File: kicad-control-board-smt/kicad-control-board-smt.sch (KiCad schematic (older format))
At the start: 97 parts, among them J101 Conn_01x10_Female, J102 Conn_01x16_Male, J103 BA56_3DIG_7SEG, J104 Gate Out, J105 Clock Out, J106 Clock In, J107 Pitch Out, J108 CV Out, J109 Reset In, Q101 MMBT3906, Q102 MMBT3906, Q103 MMBT3906, Q104 MMBT3904, Q105 MMBT3904, SW101 Shift, SW102 Play, SW103 Load, SW104 Save, SW105 Repeat, SW106 Mutate, SW107 Glide, SW108 SW_Push, SW109 SW_Push, SW110 SW_Push, SW111 SW_Push, SW112 SW_Push, SW113 SW_Push, SW114 SW_Push, SW115 SW_Push, SW116 Rotary_Encoder, SW117 SW_Push, SW118 SW_Push, SW119 SW_Push, SW120 SW_Push, SW121 SW_Push, SW122 SW_Push, SW123 SW_Push, SW124 SW_Push, U101 74HC595, U102 MCP23S17, U103 74HC595

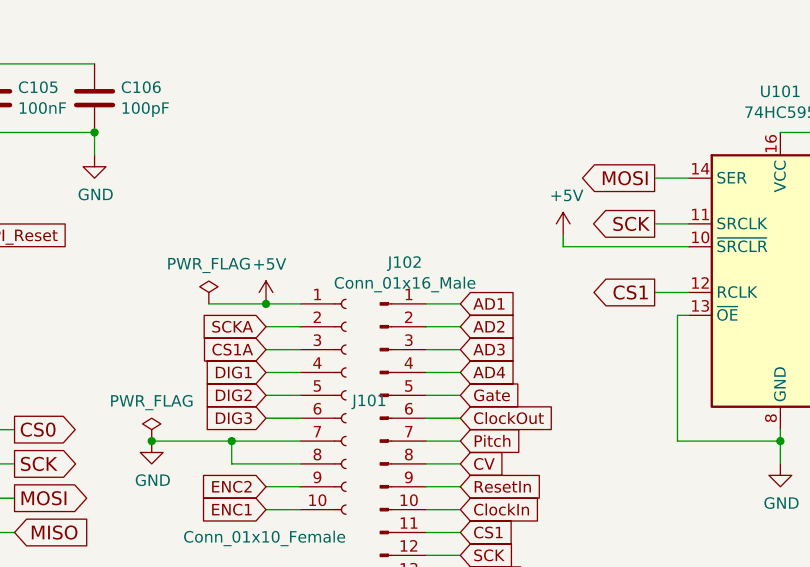
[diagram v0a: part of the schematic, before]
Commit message: Adding part numbers
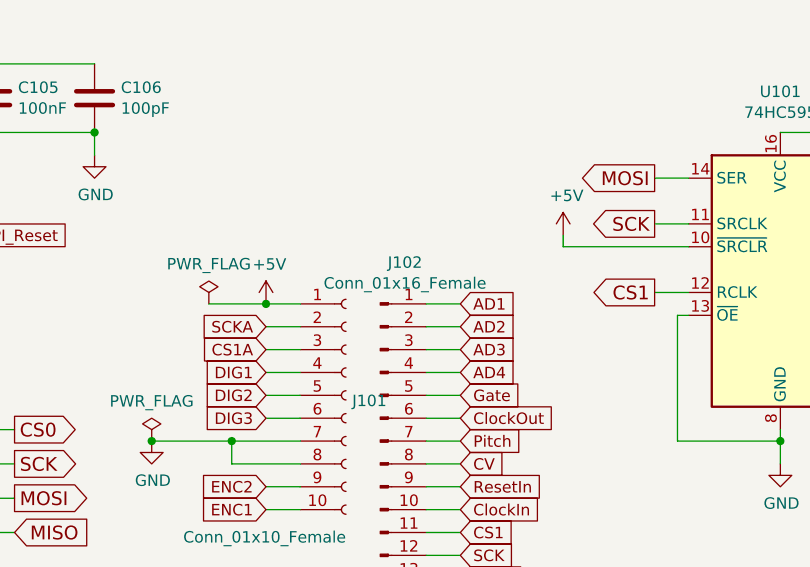
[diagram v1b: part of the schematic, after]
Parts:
- C101, C104, C107: Digikey Part Number (none) -> 493-2225-6-ND; Manufacturer Lelon -> Nichicon
- C102, C105, C108: Digikey Part Number (none) -> 399-1100-6-ND; MFG Part Number CC0603KRX7R9BB104 -> C0603C104Z3VACTU; Manufacturer Yageo -> Kemet
- C103, C106, C109: Digikey Part Number (none) -> 399-7821-6-ND; MFG Part Number CL10C101JB8NNNC -> C0603C101J1GACTU; Manufacturer Samsung -> Kemet
- D1: Digikey Part Number (none) -> TSS54URGGDKR-ND; LCSC Part Number C22452 -> (none); MFG Part Number SS54 -> TSS54U RGG; Manufacturer MDD -> Taiwan Semiconductor
- D101, D102, D103, D104, D105, D106, D107, D108, D109, D110, D111, D112, D113, D114, D115, D116, D117, D118: Digikey Part Number (none) -> C503B-AAS-CY0B0251-ND; MFG Part Number (none) -> C503B-AAS-CY0B0251; Manufacturer (none) -> Cree
- J101: Digikey Part Number (none) -> S7008-ND; MFG Part Number (none) -> PPTC101LFBN-RC; Manufacturer (none) -> Sullins
- J102: value Conn_01x16_Male -> Conn_01x16_Female; Digikey Part Number (none) -> S7014-ND; MFG Part Number (none) -> PPTC161LFBN-RC; Manufacturer (none) -> Sullins
- J103: Digikey Part Number (none) -> 754-1656-5-ND; MFG Part Number (none) -> BA56-12GWA; Manufacturer (none) -> Kingbright
- J104, J105, J106, J107, J108, J109: Digikey Part Number (none) -> N/A; MFG Part Number (none) -> WQP-WQP518MA; Manufacturer (none) -> Qingpu
- Q101, Q102, Q103: Digikey Part Number (none) -> MMBT3906LT1GOSDKR-ND; Manufacturer On Semicon -> ON Semiconductor
- Q104, Q105: Digikey Part Number (none) -> MMBT3904LT3GOSDKR-ND; MFG Part Number MMBT3904 -> MMBT3904LT3G; Manufacturer Changjiang -> ON Semiconductor
- R101, R102, R104, R105, R106, R107, R108, R109, R110, R111, R112, R113: Digikey Part Number (none) -> RMCF0603FT100RDKR-ND; MFG Part Number 0603WAF1000T5E -> RMCF0603FT100R; Manufacturer Uniroyal -> Stackpole Electronics Inc
- R103, R114, R118: Digikey Part Number (none) -> RMCF0603FT1K00DKR-ND; LCSC Part Number C21190 -> (none); MFG Part Number 0603WAF1001T5E -> RMCF0603FT1K00; Manufacturer Uniroyal -> Stackpole Electronics Inc
- R115, R116, R117: Digikey Part Number (none) -> RMCF0603FT680RCT-ND; MFG Part Number 0603WAF6800T5E -> RMCF0603FT680R; Manufacturer Uniroyal -> Stackpole Electronics Inc
- R119, R122: Digikey Part Number (none) -> RMCF0603FT10K0DKR-ND; MFG Part Number 0603WAF1002T5E -> RMCF0603FT10K0; Manufacturer Uniroyal -> Stackpole Electronics Inc
- R120, R123: Digikey Part Number (none) -> RMCF0603FG100KDKR-ND; MFG Part Number 0603WAF1003T5E -> RMCF0603FG100K; Manufacturer Uniroyal -> Stackpole Electronics Inc
- R121, R124: Digikey Part Number (none) -> RMCF0603FT1M00DKR-ND; MFG Part Number 0603WAF1004T5E -> RMCF0603FT1M00; Manufacturer Uniroyal -> Stackpole Electronics Inc
- RV101, RV102, RV103, RV104: Digikey Part Number (none) -> N/A; MFG Part Number (none) -> RV09AF-40-20K-B100K; Manufacturer (none) -> Alpha
- SW101, SW102, SW103, SW104, SW107, SW108, SW109, SW110, SW111, SW112, SW113, SW114, SW115, SW117, SW118, SW119, SW120, SW121, SW122, SW123, SW124: Digikey Part Number (none) -> EG1861-ND; MFG Part Number (none) -> TL1105SPF160Q; Manufacturer (none) -> E-Switch
- SW105, SW106: Digikey Part Number (none) -> 401-1992-ND; MFG Part Number (none) -> D6R40 F2 LFS; Manufacturer (none) -> C&K
- SW116: Digikey Part Number (none) -> PEC11R-4215F-N0024-ND; MFG Part Number (none) -> PEC11R-4215F-N0024; Manufacturer (none) -> Bourns, Inc
- U101, U103: Digikey Part Number (none) -> 1727-2821-6-ND; Manufacturer Nexperia -> Nexperia USA, Inc
- U102: Digikey Part Number (none) -> MCP23S17-E/SO-ND

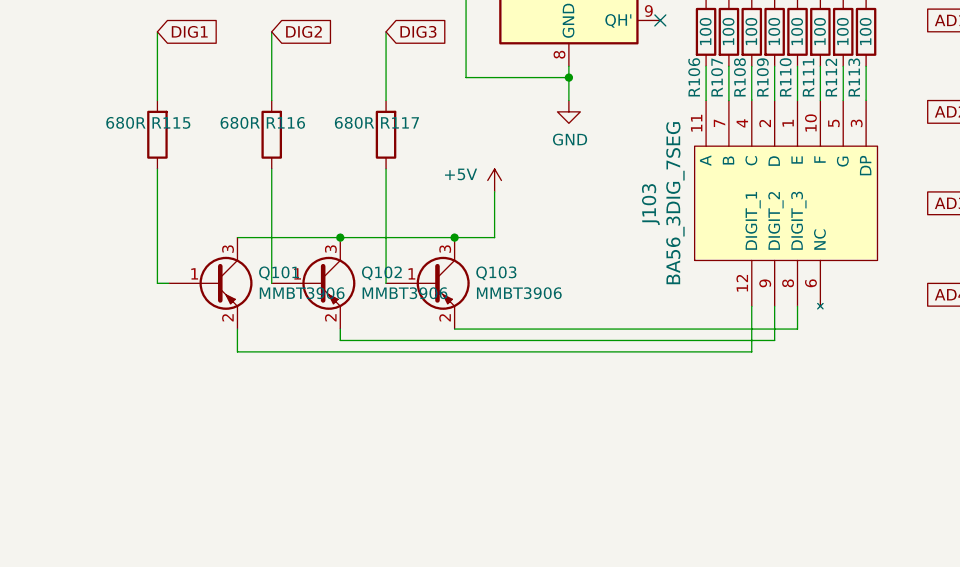
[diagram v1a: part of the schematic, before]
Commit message: Flipping SMT MMBT2N3906 transistor orientation
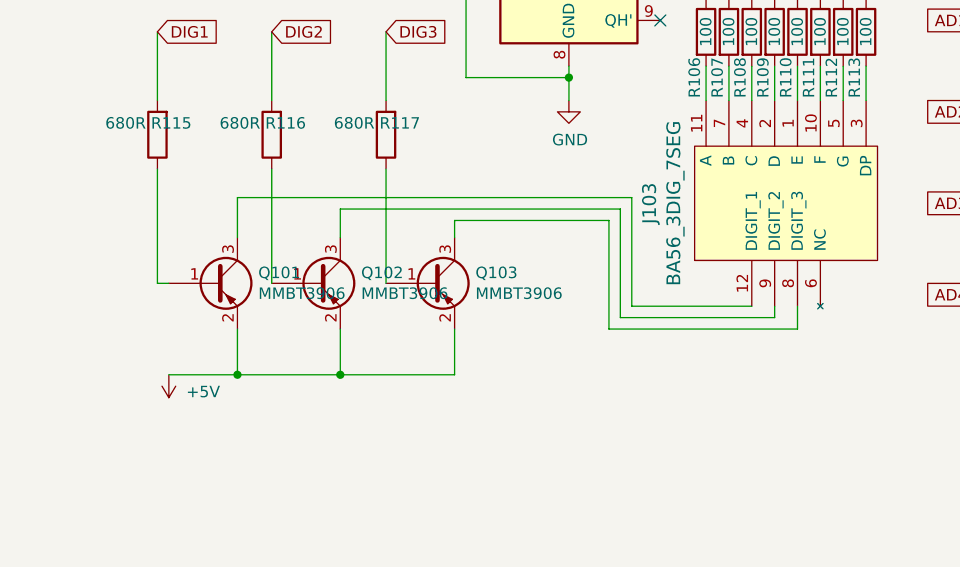
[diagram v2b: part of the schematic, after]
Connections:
- net +5V: now also Q101.2 (E), Q102.2 (E), Q103.2 (E); no longer Q101.3 (C), Q102.3 (C), Q103.3 (C)
- net at J103.12 (DIGIT_1): now also Q101.3 (C); no longer Q101.2 (E)
- net at J103.8 (DIGIT_3): now also Q103.3 (C); no longer Q103.2 (E)
- net at J103.9 (DIGIT_2): now also Q102.3 (C); no longer Q102.2 (E)
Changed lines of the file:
@@
 Wire Wire Line
 	1500 2750 3700 2750
-$Comp
-L power:+5V #PWR0118
-U 1 1 5DC2EE30
-P 8025 5550
-F 0 "#PWR0118" H 8025 5400 50  0001 C CNN
-F 1 "+5V" H 7875 5625 50  0000 C CNN
-F 2 "" H 8025 5550 50  0001 C CNN
-F 3 "" H 8025 5550 50  0001 C CNN
-	1    8025 5550
-	1    0    0    -1
-$EndComp
 Wire Wire Line
 	5700 3900 5700 3800
@@
 	6150 3700 6350 3700
 Wire Wire Line
-	6900 6250 6900 6150
-Wire Wire Line
 	6550 5150 6550 4850
 Text GLabel 7550 4850 2    50   Input ~ 0
@@
 Text GLabel 6550 4850 2    50   Input ~ 0
 DIG1
-Wire Wire Line
-	9150 6250 9150 6050
-Wire Wire Line
-	6900 6250 9150 6250
-Wire Wire Line
-	7350 6150 7350 6200
-Wire Wire Line
-	7350 6200 9250 6200
-Wire Wire Line
-	9250 6050 9250 6200
-Wire Wire Line
-	7850 6150 9350 6150
-Wire Wire Line
-	8025 5550 8025 5750
 $Comp
 L Connector:Conn_01x16_Male J102
@@
 Connection ~ 2200 7350
 Connection ~ 2500 7550
-Wire Wire Line
-	6900 5750 7350 5750
-Connection ~ 7350 5750
-Wire Wire Line
-	7350 5750 7850 5750
-Connection ~ 7850 5750
-Wire Wire Line
-	7850 5750 8025 5750
 $Comp
 L Device:D_Schottky D1
@@
 Wire Wire Line
 	3450 5350 3700 5350
+$Comp
+L power:+5V #PWR0118
+U 1 1 5DC2EE30
+P 6600 6350
+F 0 "#PWR0118" H 6600 6200 50  0001 C CNN
+F 1 "+5V" H 6450 6425 50  0000 C CNN
+F 2 "" H 6600 6350 50  0001 C CNN
+F 3 "" H 6600 6350 50  0001 C CNN
+	1    6600 6350
+	-1   0    0    1
+$EndComp
+Wire Wire Line
+	7850 6350 7850 6150
+Wire Wire Line
+	7350 6150 7350 6350
+Wire Wire Line
+	7350 6350 7850 6350
+Connection ~ 7350 6350
+Wire Wire Line
+	6900 6150 6900 6350
+Wire Wire Line
+	6600 6350 6900 6350
+Wire Wire Line
+	6900 6350 7350 6350
+Connection ~ 6900 6350
+Wire Wire Line
+	9350 6150 8525 6150
+Wire Wire Line
+	8525 6150 8525 5675
+Wire Wire Line
+	8525 5675 7850 5675
+Wire Wire Line
+	7850 5675 7850 5750
+Wire Wire Line
+	9250 6050 9250 6100
+Wire Wire Line
+	9250 6100 8575 6100
+Wire Wire Line
+	8575 6100 8575 5625
+Wire Wire Line
+	8575 5625 7350 5625
+Wire Wire Line
+	7350 5625 7350 5750
+Wire Wire Line
+	9150 6050 8625 6050
+Wire Wire Line
+	8625 6050 8625 5575
+Wire Wire Line
+	8625 5575 6900 5575
+Wire Wire Line
+	6900 5575 6900 5750
 Wire Bus Line
 	3050 850  3050 1550
